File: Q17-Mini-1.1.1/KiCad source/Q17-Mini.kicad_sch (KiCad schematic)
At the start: 80 parts, among them J1 Input, J2-1 SPK+, J2-2 SPK-, J3-1 V+, J3-2 GND, J3-3 V-, Q1 IRF610, Q10 KSA992, Q11 ZVP2106A, Q12 BD139, Q13 IRF610, Q14 IRF9610, Q15 FQA46N15, Q16 FQA36P15, Q2 KSA992, Q3 KSC1845, Q4 IRF9610, Q5 FQP3P20, Q6 FQP3N30, Q7 KSC1845, Q8 ZVN4206AV, Q9 ZVP2106A, U1 OPA1641

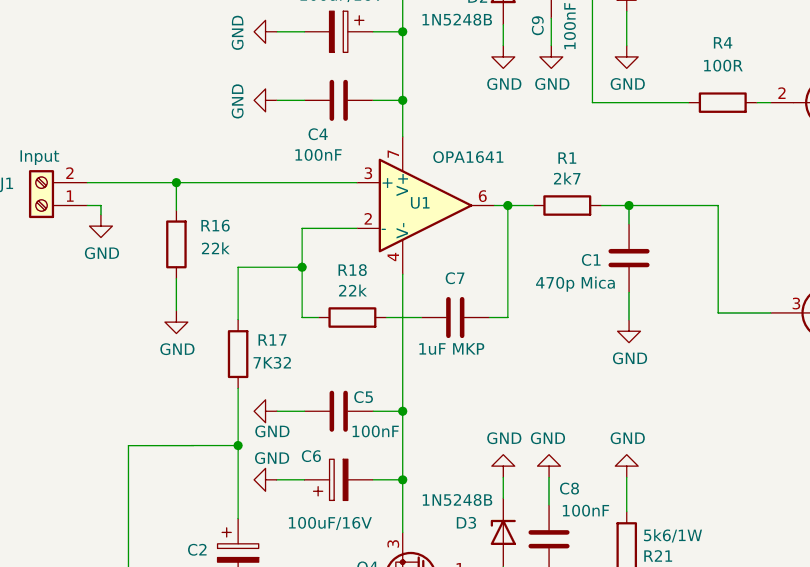
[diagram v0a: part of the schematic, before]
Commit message: Q17-Mini-1.1.2 release
- New vertical footprint for coil
- New SMD footprints on back PCB
- Update C7/R18 circuit position
- Some tracks optimisation
- New 3D and PCB pictures
- Archived version 1.1.1
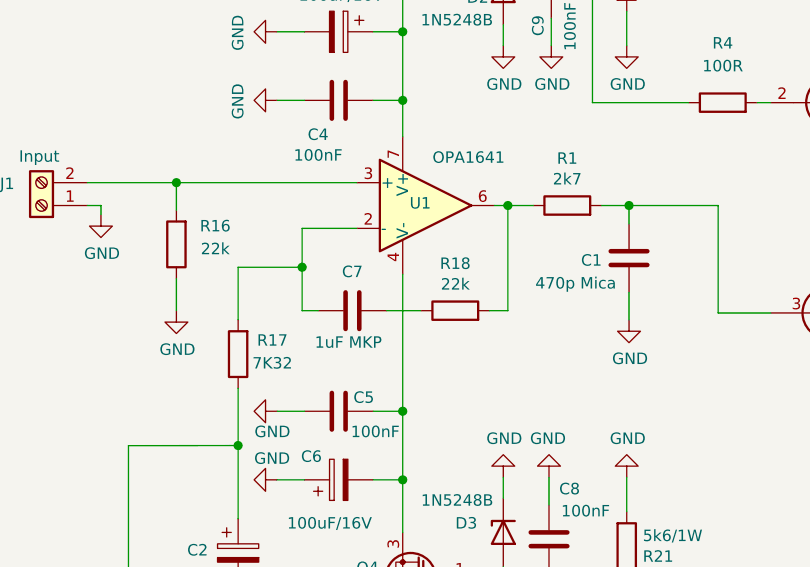
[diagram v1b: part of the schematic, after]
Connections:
- net at R1.1, U1.6: now also R18.2; no longer C7.2
- net at C7.1: now also R17.2, U1.2 (-); no longer R18.2
- new net: C7.2, R18.1
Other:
- moved on the sheet: C7, R18
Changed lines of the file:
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@@
   (title_block
     (title "Q17-Mini Amplifier")
-    (date "2022-01-04")
-    (rev "1.2.3")
+    (date "2022-01-02")
+    (rev "1.2.2")
     (company "by eng. Tiberiu Vicol")
     (comment 1 "Modified by Stef for the Q17-Mini project")
@@
     (stroke (width 0) (type solid) (color 0 0 0 0))
   )
-  (wire (pts (xy 77.47 88.9) (xy 79.502 88.9))
-    (stroke (width 0) (type default) (color 0 0 0 0))
-  )
   (wire (pts (xy 92.71 40.894) (xy 92.71 38.1))
     (stroke (width 0) (type solid) (color 0 0 0 0))
@@
     (stroke (width 0) (type solid) (color 0 0 0 0))
   )
-  (wire (pts (xy 58.42 88.9) (xy 56.642 88.9))
-    (stroke (width 0) (type default) (color 0 0 0 0))
-  )
   (wire (pts (xy 92.71 124.46) (xy 92.71 118.11))
     (stroke (width 0) (type solid) (color 0 0 0 0))
@@
     (stroke (width 0) (type solid) (color 0 0 0 0))
   )
-  (wire (pts (xy 56.642 83.312) (xy 56.642 88.9))
+  (wire (pts (xy 58.42 88.138) (xy 56.642 88.138))
+    (stroke (width 0) (type solid) (color 0 0 0 0))
+  )
+  (wire (pts (xy 56.642 88.138) (xy 56.642 83.312))
     (stroke (width 0) (type solid) (color 0 0 0 0))
   )
@@
     (stroke (width 0) (type solid) (color 0 0 0 0))
   )
-  (wire (pts (xy 79.502 76.454) (xy 79.502 88.9))
+  (wire (pts (xy 79.502 88.138) (xy 79.502 76.454))
+    (stroke (width 0) (type solid) (color 0 0 0 0))
+  )
+  (wire (pts (xy 77.47 88.138) (xy 79.502 88.138))
     (stroke (width 0) (type solid) (color 0 0 0 0))
   )
@@
     (stroke (width 0) (type solid) (color 0 0 0 0))
   )
-  (wire (pts (xy 66.04 88.9) (xy 69.85 88.9))
-    (stroke (width 0) (type default) (color 0 0 0 0))
-  )
   (wire (pts (xy 127.762 47.244) (xy 123.952 47.244))
     (stroke (width 0) (type solid) (color 0 0 0 0))
@@
   )
   (wire (pts (xy 194.31 139.7) (xy 194.31 141.478))
+    (stroke (width 0) (type solid) (color 0 0 0 0))
+  )
+  (wire (pts (xy 66.04 88.138) (xy 69.85 88.138))
     (stroke (width 0) (type solid) (color 0 0 0 0))
   )
@@
     (pin "3")
   )
-  (symbol (lib_name "C_1") (lib_id "Device:C") (at 73.66 88.9 90) (unit 1)
-    (in_bom yes) (on_board yes)
-    (property "Reference" "C7" (id 0) (at 73.66 84.582 90))
-    (property "Value" "1uF MKP" (id 1) (at 73.2055 92.4302 90))
-    (property "Footprint" "Capacitor_THT:C_Rect_C7_Q17-Mini" (id 2) (at 77.47 87.9348 0)
-      (effects (font (size 1.27 1.27)) hide)
-    )
-    (property "Datasheet" "~" (id 3) (at 73.66 88.9 0)
+  (symbol (lib_name "C_1") (lib_id "Device:C") (at 62.23 88.138 90) (unit 1)
+    (in_bom yes) (on_board yes)
+    (property "Reference" "C7" (id 0) (at 62.23 83.82 90))
+    (property "Value" "1uF MKP" (id 1) (at 61.7755 91.6682 90))
+    (property "Footprint" "Capacitor_THT:C_Rect_C7_Q17-Mini" (id 2) (at 66.04 87.1728 0)
+      (effects (font (size 1.27 1.27)) hide)
+    )
+    (property "Datasheet" "~" (id 3) (at 62.23 88.138 0)
       (effects (font (size 1.27 1.27)) hide)
     )
@@
     (pin "3")
   )
-  (symbol (lib_name "R_1") (lib_id "Device:R") (at 62.23 88.9 90) (unit 1)
-    (in_bom yes) (on_board yes)
-    (property "Reference" "R18" (id 0) (at 62.23 83.6738 90))
-    (property "Value" "22k" (id 1) (at 62.23 85.9725 90))
-    (property "Footprint" "Resistor_THT:R_Axial_DIN0207_L6.3mm_D2.5mm_P10.16mm_Horizontal" (id 2) (at 62.23 90.678 90)
-      (effects (font (size 1.27 1.27)) hide)
-    )
-    (property "Datasheet" "~" (id 3) (at 62.23 88.9 0)
-      (effects (font (size 1.27 1.27)) hide)
-    )
+  (symbol (lib_name "R_1") (lib_id "Device:R") (at 73.66 88.138 90) (unit 1)
+    (in_bom yes) (on_board yes)
+    (property "Reference" "R18" (id 0) (at 73.66 82.9118 90))
+    (property "Value" "22k" (id 1) (at 73.66 85.2105 90))
+    (property "Footprint" "Resistor_THT:R_Axial_DIN0207_L6.3mm_D2.5mm_P10.16mm_Horizontal" (id 2) (at 73.66 89.916 90)
+      (effects (font (size 1.27 1.27)) hide)
+    )
+    (property "Datasheet" "~" (id 3) (at 73.66 88.138 0)
+      (effects (font (size 1.27 1.27)) hide)
+    )
